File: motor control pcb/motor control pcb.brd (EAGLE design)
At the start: 35.6 x 17.8 mm, 26 parts, among them IC4 SN75176ASOIC, IC5 ATMEGA328

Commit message: Update board again.
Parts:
- moved C1 8.83 mm to (24.7, 20.5), turned to 180 degrees
- moved C5 5.86 mm to (4.80, 0.46)
- moved C2 4.94 mm to (24.0, 0.41), turned to 180 degrees
- moved R5 2.26 mm to (18.4, 14.6)
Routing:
- net A7: track 38.3 -> 48.7 mm
- net VCC: track 158.1 -> 150.6 mm, vias 10 -> 4
- net D9: track 11.1 -> 13.4 mm
- net D11: track 30.4 -> 31.8 mm, vias 2 -> 1
- net GND: track 210.3 -> 209.2 mm, vias 6 -> 3
- net D13: track 29.0 -> 28.0 mm
- net RS485A: track 22.5 -> 22.3 mm, vias 2 -> 1
- net RS485B: track 27.3 -> 27.2 mm, vias 2 -> 1

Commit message: Rearrange things.
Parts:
- moved R7 9.06 mm to (29.0, 42.6)
- moved C7 7.64 mm to (24.2, 42.6)
- moved ICSP 6.39 mm to (35.5, 41.3)
- moved MOTOR 4.83 mm to (20.5, 2.82)
- moved R4 4.83 mm to (24.0, 17.4)
- moved R5 4.83 mm to (22.4, 17.4)
- moved C5 4.83 mm to (8.74, 3.25)
- moved U$1 4.83 mm to (6.53, 22.3)
- moved C8 4.83 mm to (39.2, 18.5)
- moved C2 4.83 mm to (27.9, 3.20)
- moved POT 4.83 mm to (36.2, 2.87)
- moved R1 4.03 mm to (24.4, 39.5)
- moved DEBUG 3.83 mm to (6.60, 35.0)
- moved R8 3.83 mm to (9.58, 35.0)
- moved C3 3.83 mm to (11.8, 30.8)
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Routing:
- net GND: track 209.2 -> 220.7 mm, vias 3 -> 4
- net N$11: track 10.2 -> 14.6 mm
- net RESET: track 24.5 -> 20.8 mm
- net D11: track 31.8 -> 35.2 mm
- net VMOT: track 62.0 -> 60.5 mm
- net D13: track 28.0 -> 29.2 mm
- net VCC: track 150.6 -> 149.9 mm, vias 4 -> 5
- net A3: track 12.3 -> 11.8 mm
- added copper zone on layer 1, net N$1
- removed copper zone on layer 1, net GND
- removed copper zone on layer 16, net GND
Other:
- board outline removed

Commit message: Board layout finished, need verification
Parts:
- added C6: ?pf, SparkFun:0805
- C1, C2: value 16pf -> ?pf
- C8: value 100nF -> ?pf; device SparkFun:0805 -> SparkFun:1210
- R2, R3: value 4.7k -> 10k
- R4: value 1K -> ?k
- R5: value 4.7k -> ?k
- moved C1 20.6 mm to (4.65, 16.8), turned to 90 degrees
- moved R4 17.6 mm to (6.43, 16.8)
- moved R5 16.1 mm to (6.43, 19.8), turned to 270 degrees
- moved C8 7.93 mm to (47.1, 18.7), turned to 0 degrees
- moved C2 2.13 mm to (29.9, 2.41)
- moved C5 2.10 mm to (10.7, 2.41)
- moved POT 2.01 mm to (38.2, 2.41)
- moved U$1 2.00 mm to (8.48, 21.9)
- moved MOTOR 2.00 mm to (22.5, 2.41)
- moved C12 1.65 mm to (4.95, 29.8)
- moved C13 1.65 mm to (4.95, 26.6)
- moved Q1 1.63 mm to (8.31, 28.0)
- moved C4 1.54 mm to (26.6, 24.8)
- moved DEBUG 0.97 mm to (5.64, 34.9)
- moved R8 0.97 mm to (8.61, 34.9)
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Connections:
- net GND: now also C6.1
- net VCC: no longer C8.2
- net VMOT: now also C6.2, C8.2
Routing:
- net GND: track 220.7 -> 235.1 mm
- net N$11: track 14.6 -> 27.4 mm, vias 0 -> 2
- net D13: track 29.2 -> 24.0 mm
- net D5: track 13.2 -> 8.23 mm
- net D6: track 11.5 -> 6.68 mm
- net VMOT: track 60.5 -> 64.4 mm
- net D9: track 13.7 -> 16.3 mm, vias 0 -> 2
- net A7: track 48.4 -> 50.7 mm
- net D11: track 35.2 -> 37.4 mm
- net D7: track 7.13 -> 5.46 mm
- net D12: track 38.5 -> 36.9 mm
- net VCC: track 149.9 -> 148.4 mm, vias 5 -> 4
- net D10: track 5.18 -> 6.58 mm
- net N$6: track 11.0 -> 12.3 mm
- net RS485A: track 21.8 -> 20.8 mm
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
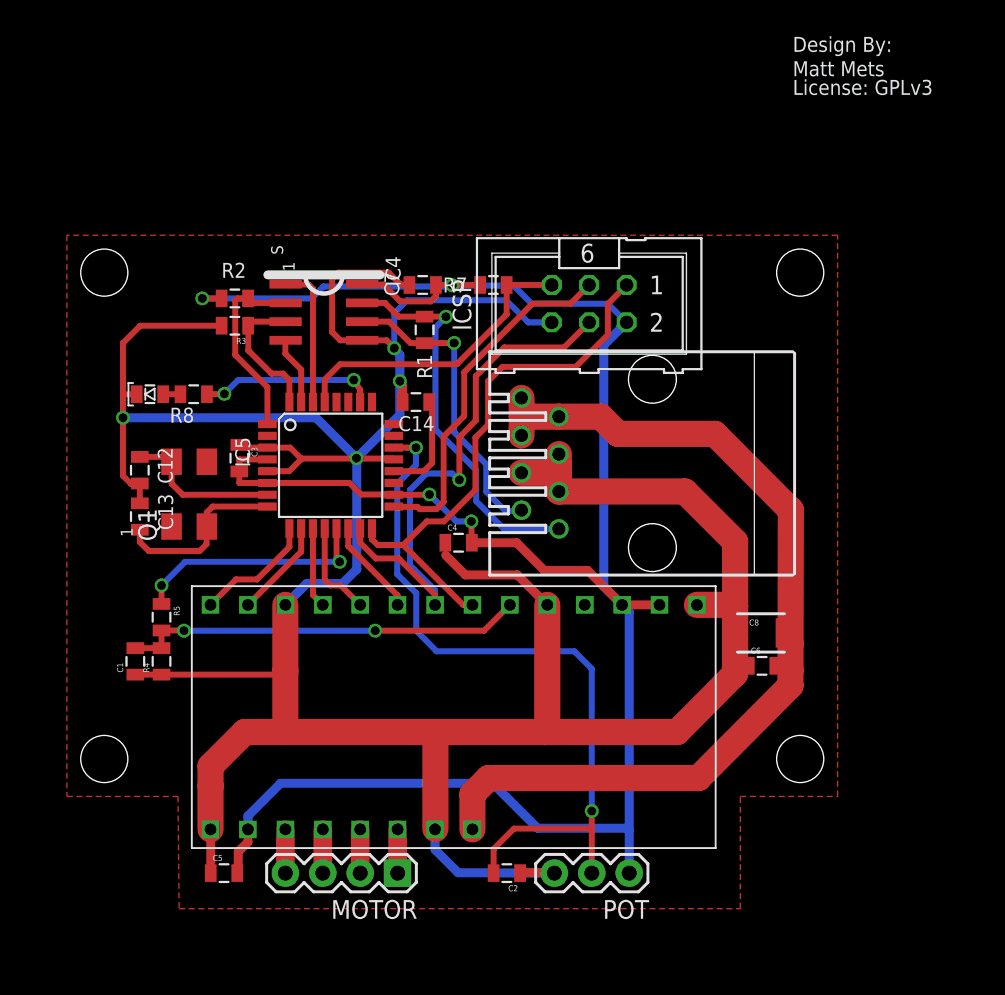
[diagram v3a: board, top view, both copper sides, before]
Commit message: Finish laying out and verifying board. Bugfix: don't pull /sleep low.
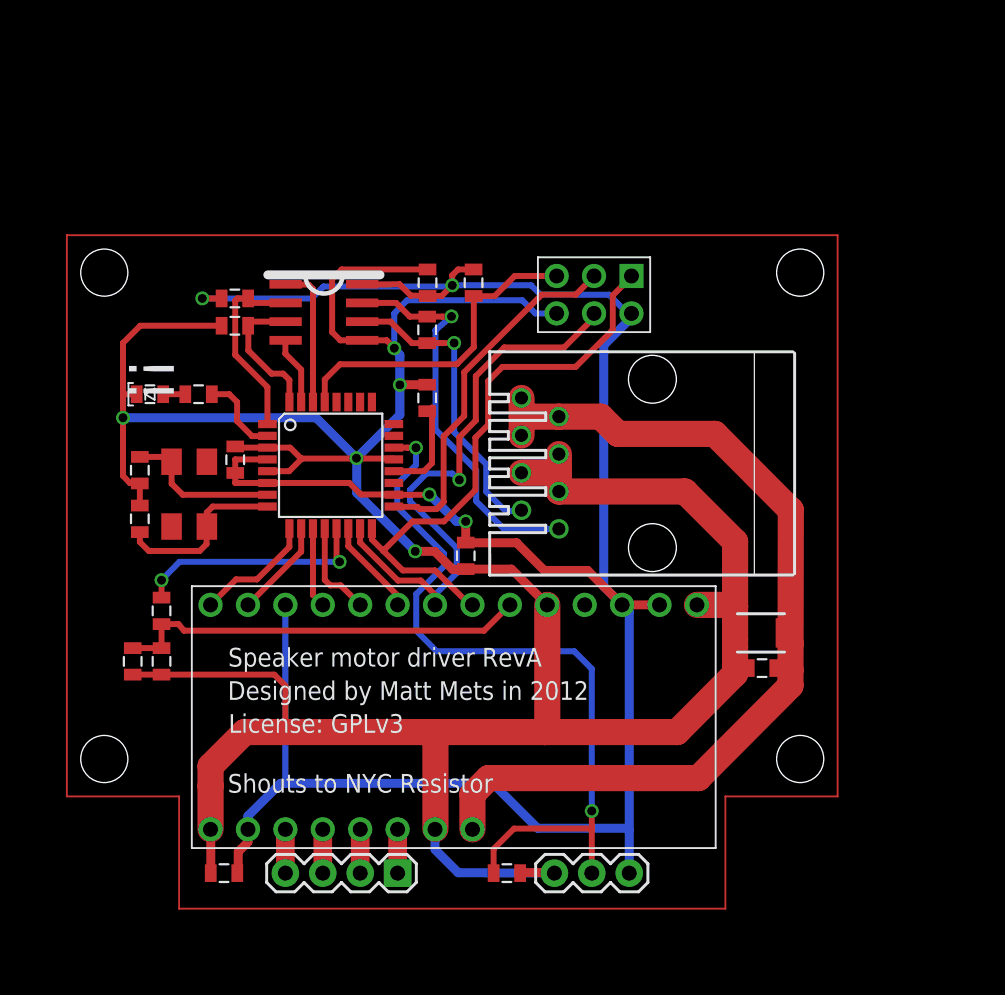
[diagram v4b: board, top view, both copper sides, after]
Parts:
- removed ICSP: (no value), con-harting-ml:ML6
- added U$2: 2X3HEADER, sonos_library:2X3HEADER
- moved R7 1.35 mm to (27.6, 42.5), turned to 90 degrees
- moved C4 1.01 mm to (27.1, 24.0), turned to 90 degrees
- moved C14 0.81 mm to (24.5, 34.7), turned to 270 degrees
- moved R5 0.43 mm to (6.43, 20.2)
- moved C7 0.36 mm to (24.5, 42.5), turned to 270 degrees
- moved R8 0.33 mm to (8.94, 34.9)
- moved C3 0.30 mm to (11.4, 30.5)
- moved R1 0.18 mm to (24.5, 39.3)
- moved C1 0.18 mm to (4.47, 16.8)
- moved C13 0.15 mm to (4.95, 26.5)
- moved C6 0.15 mm to (47.2, 16.3)
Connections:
- net A3: no longer R8.2
- net D11: now also U$2.P$4; no longer ICSP.4
- net D12: now also U$2.P$1; no longer ICSP.1
- net D13: now also U$2.P$3; no longer ICSP.3
- net D4: now also R8.2
- net GND: now also U$2.P$6; no longer ICSP.6, U$1./SLP
- net RESET: now also U$2.P$5; no longer ICSP.5
- net VCC: now also U$1./SLP, U$2.P$2; no longer ICSP.2
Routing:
- net N$7: track 0.00 -> 196.1 mm
- net VCC: track 148.4 -> 161.6 mm
- net A3: track 12.0 -> 0.00 mm, vias 2 -> 0
- net GND: track 235.1 -> 228.8 mm, vias 4 -> 5
- net D4: track 0.00 -> 5.72 mm
- net D12: track 36.9 -> 39.2 mm
- net D11: track 37.4 -> 39.4 mm
- net A7: track 50.7 -> 52.3 mm
- net RESET: track 20.8 -> 22.2 mm
- net N$11: track 27.4 -> 28.2 mm, vias 2 -> 0
- net RS485B: track 26.4 -> 27.0 mm
- net D13: track 24.0 -> 24.6 mm
- removed copper zone on layer 1, net N$1
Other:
- board text added: "!!"
- board text added: "Designed by Matt Mets in 2012"
- board text added: "Shouts to NYC Resistor"
- board text added: "Speaker motor driver RevA"
- board text removed: "1"
- board text removed: "Design By:"
- board text removed: "Matt Mets"
- board text removed: "S"
